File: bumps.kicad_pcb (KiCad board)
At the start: 2 copper layers, 111.1 x 65.4 mm, 132 parts, among them M1 CONN_1, M2 CONN_1, M3 CONN_1, P1 DIL6, P10 Mot-A, P11 Mot-A, P12 Mot-X, P13 T1, P14 T2, P15 T3, P16 MPower, P17 PWM-2, P18 PWM-1, P19 END-X, P2 DIL6, P20 END-Y, P21 END-Z, P22 Mot-X, P23 Mot-Y, P24 Mot-Y, P25 Mot-Z, P26 Mot-Z, P27 Aux, P28 KillSwitch, P29 PWM, P3 Mot-E, P4 Mot-E, P5 DIL6, P6 DIL6, P7 DIL6, P8 P8 Header, P9 P9 Header, Q1 IRLB8743PBF, Q2 IRLB8743PBF, Q3 FDS9926A, Q4 FDS9926A, U1 Motor-2, U2 Motor-4, U3 Motor-5, U4 Motor-3, U5 Motor-1, U6 MC34063, U7 AP1117/3.3, U8 Opto

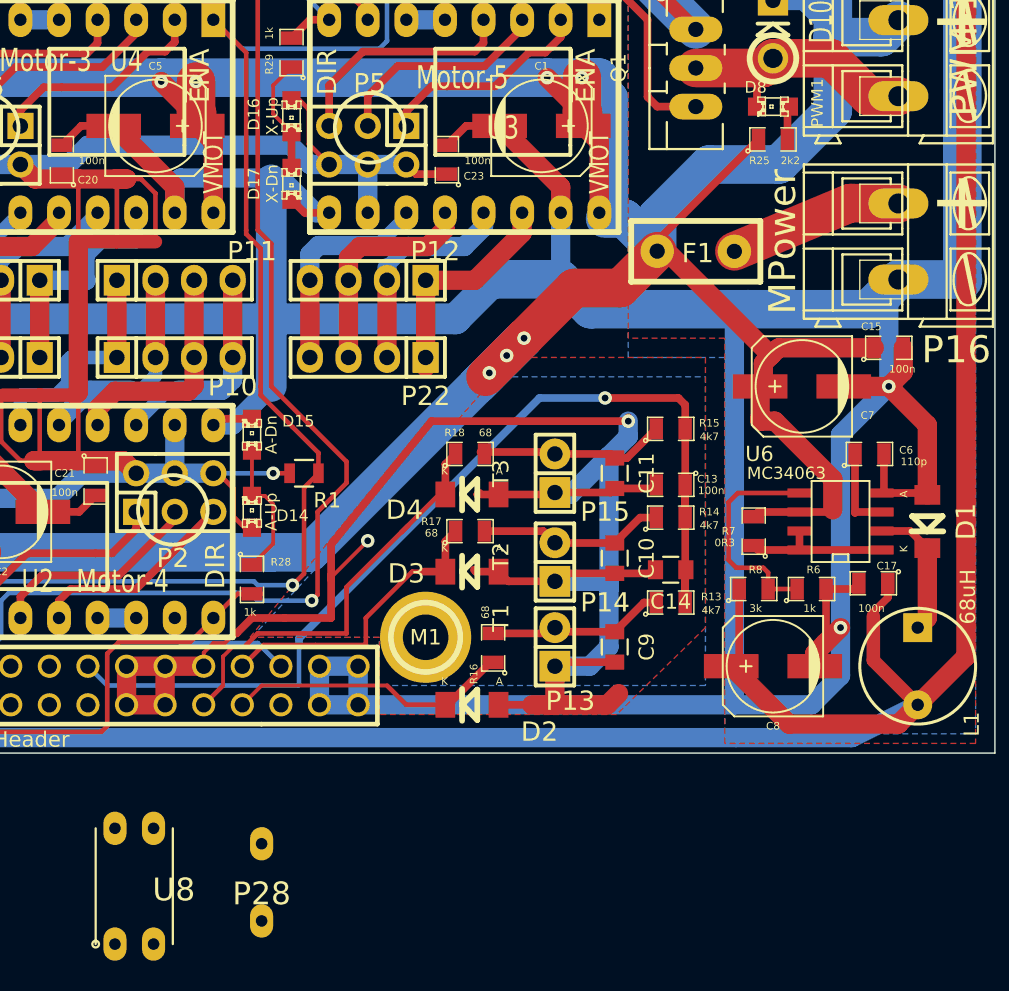
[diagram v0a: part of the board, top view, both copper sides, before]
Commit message: o Adding fuse holder (footprint and schematic). o .. work in progress. Attempt to make things fit.
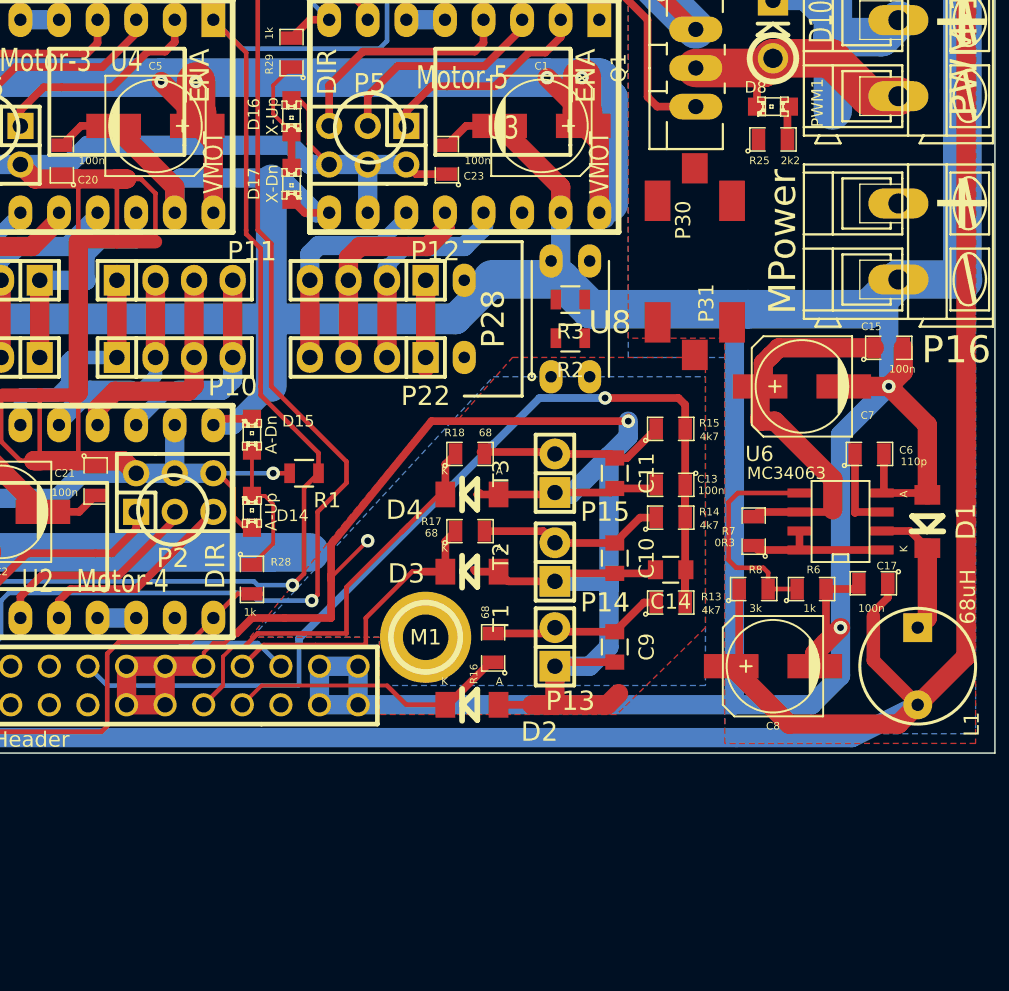
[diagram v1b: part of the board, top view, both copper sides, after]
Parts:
- removed F1: FUSE, Fuse_Holders_and_Fuses:Fuse_TE5_Littlefuse-395Series
- added P30: CONN_01X01, bumps:FuseBlade, F.Cu at (139.0, 57.0)
- added P31: CONN_01X01, bumps:FuseBlade, F.Cu at (139.0, 65.0)
- added R2: 330, Resistors_SMD:R_0805, F.Cu at (130.8, 66.0)
- added R3: 4k7, Resistors_SMD:R_0805, F.Cu at (130.8, 63.5)
- moved U8 47.1 mm to (130.8, 64.8)
- moved P28 39.4 mm to (123.8, 64.8), turned to 180 degrees
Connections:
- M1 pad 1: (no net) -> Net-(M1-Pad1)
- M2 pad 1: (no net) -> Net-(M2-Pad1)
- M3 pad 1: (no net) -> Net-(M3-Pad1)
- P8 pad 18: (no net) -> Net-(P8-Pad18)
- P8 pad 19: (no net) -> Net-(P8-Pad19)
- P8 pad 20: (no net) -> Net-(P8-Pad20)
- P8 pad 21: (no net) -> Net-(P8-Pad21)
- P8 pad 22: (no net) -> Net-(P8-Pad22)
- P8 pad 23: (no net) -> Net-(P8-Pad23)
- P8 pad 24: (no net) -> Net-(P8-Pad24)
- P8 pad 25: (no net) -> Net-(P8-Pad25)
- P8 pad 26: (no net) -> Net-(P8-Pad26)
- P8 pad 27: (no net) -> Net-(P8-Pad27)
- P8 pad 28: (no net) -> Net-(P8-Pad28)
- P8 pad 29: (no net) -> Net-(P8-Pad29)
- P8 pad 3: (no net) -> Net-(P8-Pad3)
- P8 pad 30: (no net) -> Net-(P8-Pad30)
- P8 pad 31: (no net) -> Net-(P8-Pad31)
- P8 pad 32: (no net) -> Net-(P8-Pad32)
- P8 pad 33: (no net) -> Net-(P8-Pad33)
- P8 pad 34: (no net) -> Net-(P8-Pad34)
- P8 pad 35: (no net) -> Net-(P8-Pad35)
- P8 pad 36: (no net) -> Net-(P8-Pad36)
- P8 pad 37: (no net) -> Net-(P8-Pad37)
- P8 pad 38: (no net) -> Net-(P8-Pad38)
- P8 pad 39: (no net) -> Net-(P8-Pad39)
- P8 pad 4: (no net) -> Net-(P8-Pad4)
- P8 pad 40: (no net) -> Net-(P8-Pad40)
- P8 pad 41: (no net) -> Net-(P8-Pad41)
- P8 pad 42: (no net) -> Net-(P8-Pad42)
- P8 pad 43: (no net) -> Net-(P8-Pad43)
- P8 pad 44: (no net) -> Net-(P8-Pad44)
- P8 pad 45: (no net) -> Net-(P8-Pad45)
- P8 pad 46: (no net) -> Net-(P8-Pad46)
- P8 pad 5: (no net) -> Net-(P8-Pad5)
- P8 pad 6: (no net) -> Net-(P8-Pad6)
- P9 pad 10: (no net) -> Net-(P9-Pad10)
- P9 pad 14: (no net) -> DIR_C
- P9 pad 16: (no net) -> DIR_U
- P9 pad 19: (no net) -> Net-(P9-Pad19)
- P9 pad 20: (no net) -> Net-(P9-Pad20)
- P9 pad 23: (no net) -> DIR_B
- P9 pad 24: (no net) -> STEP_C
- P9 pad 25: (no net) -> Net-(P9-Pad25)
- P9 pad 26: (no net) -> STEP_B
- P9 pad 27: (no net) -> Net-(P9-Pad27)
- P9 pad 28: (no net) -> Net-(P9-Pad28)
- P9 pad 29: (no net) -> Net-(P9-Pad29)
- P9 pad 3: (no net) -> Net-(P9-Pad3)
- P9 pad 30: (no net) -> Net-(P9-Pad30)
- P9 pad 31: (no net) -> Net-(P9-Pad31)
- P9 pad 4: (no net) -> Net-(P9-Pad4)
- P9 pad 41: (no net) -> STEP_U
- P9 pad 7: (no net) -> Net-(P9-Pad7)
- P9 pad 8: (no net) -> Net-(P9-Pad8)
- P9 pad 9: (no net) -> Net-(P9-Pad9)
- U8 pad 1: (no net) -> Net-(R2-Pad2)
- U8 pad 3: (no net) -> ~EStop
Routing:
- net VMOT: track 329.1 -> 247.3 mm, vias 13 -> 10
- net Net-(P16-Pad1): track 11.4 -> 0.00 mm
- net Net-(P12-Pad1): track 14.7 -> 5.71 mm

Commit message: o intermediate state.
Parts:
- U8: moved to B.Cu
- turned P28 to 0 degrees
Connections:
- M1 pad 1: Net-(M1-Pad1) -> (no net)
- M2 pad 1: Net-(M2-Pad1) -> (no net)
- M3 pad 1: Net-(M3-Pad1) -> (no net)
- P8 pad 18: Net-(P8-Pad18) -> (no net)
- P8 pad 19: Net-(P8-Pad19) -> (no net)
- P8 pad 20: Net-(P8-Pad20) -> (no net)
- P8 pad 21: Net-(P8-Pad21) -> (no net)
- P8 pad 22: Net-(P8-Pad22) -> (no net)
- P8 pad 23: Net-(P8-Pad23) -> (no net)
- P8 pad 24: Net-(P8-Pad24) -> (no net)
- P8 pad 25: Net-(P8-Pad25) -> (no net)
- P8 pad 26: Net-(P8-Pad26) -> (no net)
- P8 pad 27: Net-(P8-Pad27) -> (no net)
- P8 pad 28: Net-(P8-Pad28) -> (no net)
- P8 pad 29: Net-(P8-Pad29) -> (no net)
- P8 pad 3: Net-(P8-Pad3) -> (no net)
- P8 pad 30: Net-(P8-Pad30) -> (no net)
- P8 pad 31: Net-(P8-Pad31) -> (no net)
- P8 pad 32: Net-(P8-Pad32) -> (no net)
- P8 pad 33: Net-(P8-Pad33) -> (no net)
- P8 pad 34: Net-(P8-Pad34) -> (no net)
- P8 pad 35: Net-(P8-Pad35) -> (no net)
- P8 pad 36: Net-(P8-Pad36) -> (no net)
- P8 pad 37: Net-(P8-Pad37) -> (no net)
- P8 pad 38: Net-(P8-Pad38) -> (no net)
- P8 pad 39: Net-(P8-Pad39) -> (no net)
- P8 pad 4: Net-(P8-Pad4) -> (no net)
- P8 pad 40: Net-(P8-Pad40) -> (no net)
- P8 pad 41: Net-(P8-Pad41) -> (no net)
- P8 pad 42: Net-(P8-Pad42) -> (no net)
- P8 pad 43: Net-(P8-Pad43) -> (no net)
- P8 pad 44: Net-(P8-Pad44) -> (no net)
- P8 pad 45: Net-(P8-Pad45) -> (no net)
- P8 pad 46: Net-(P8-Pad46) -> (no net)
- P8 pad 5: Net-(P8-Pad5) -> (no net)
- P8 pad 6: Net-(P8-Pad6) -> (no net)
- P9 pad 10: Net-(P9-Pad10) -> (no net)
- P9 pad 14: DIR_C -> (no net)
- P9 pad 16: DIR_U -> (no net)
- P9 pad 19: Net-(P9-Pad19) -> (no net)
- P9 pad 20: Net-(P9-Pad20) -> (no net)
- P9 pad 23: DIR_B -> (no net)
- P9 pad 24: STEP_C -> (no net)
- P9 pad 25: Net-(P9-Pad25) -> (no net)
- P9 pad 26: STEP_B -> (no net)
- P9 pad 27: Net-(P9-Pad27) -> (no net)
- P9 pad 28: Net-(P9-Pad28) -> (no net)
- P9 pad 29: Net-(P9-Pad29) -> (no net)
- P9 pad 3: Net-(P9-Pad3) -> (no net)
- P9 pad 30: Net-(P9-Pad30) -> (no net)
- P9 pad 31: Net-(P9-Pad31) -> (no net)
- P9 pad 4: Net-(P9-Pad4) -> (no net)
- P9 pad 41: STEP_U -> (no net)
- P9 pad 7: Net-(P9-Pad7) -> (no net)
- P9 pad 8: Net-(P9-Pad8) -> (no net)
- P9 pad 9: Net-(P9-Pad9) -> (no net)
- U1 pad 5: Net-(U1-Pad5) -> ~EStop
- U1 pad 6: Net-(U1-Pad5) -> (no net)
- U2 pad 5: Net-(U2-Pad5) -> ~EStop
- U2 pad 6: Net-(U2-Pad5) -> (no net)
- U3 pad 5: Net-(U3-Pad5) -> ~EStop
- U3 pad 6: Net-(U3-Pad5) -> (no net)
- U4 pad 5: Net-(U4-Pad5) -> ~EStop
- U4 pad 6: Net-(U4-Pad5) -> (no net)
- U5 pad 5: Net-(U5-Pad5) -> ~EStop
- U5 pad 6: Net-(U5-Pad5) -> (no net)
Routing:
- net Net-(U4-Pad5): track 2.54 -> 0.00 mm
- net Net-(U3-Pad5): track 2.54 -> 0.00 mm
- net Net-(U2-Pad5): track 2.54 -> 0.00 mm
- net Net-(U5-Pad5): track 2.54 -> 0.00 mm
- net Net-(U1-Pad5): track 2.54 -> 0.00 mm

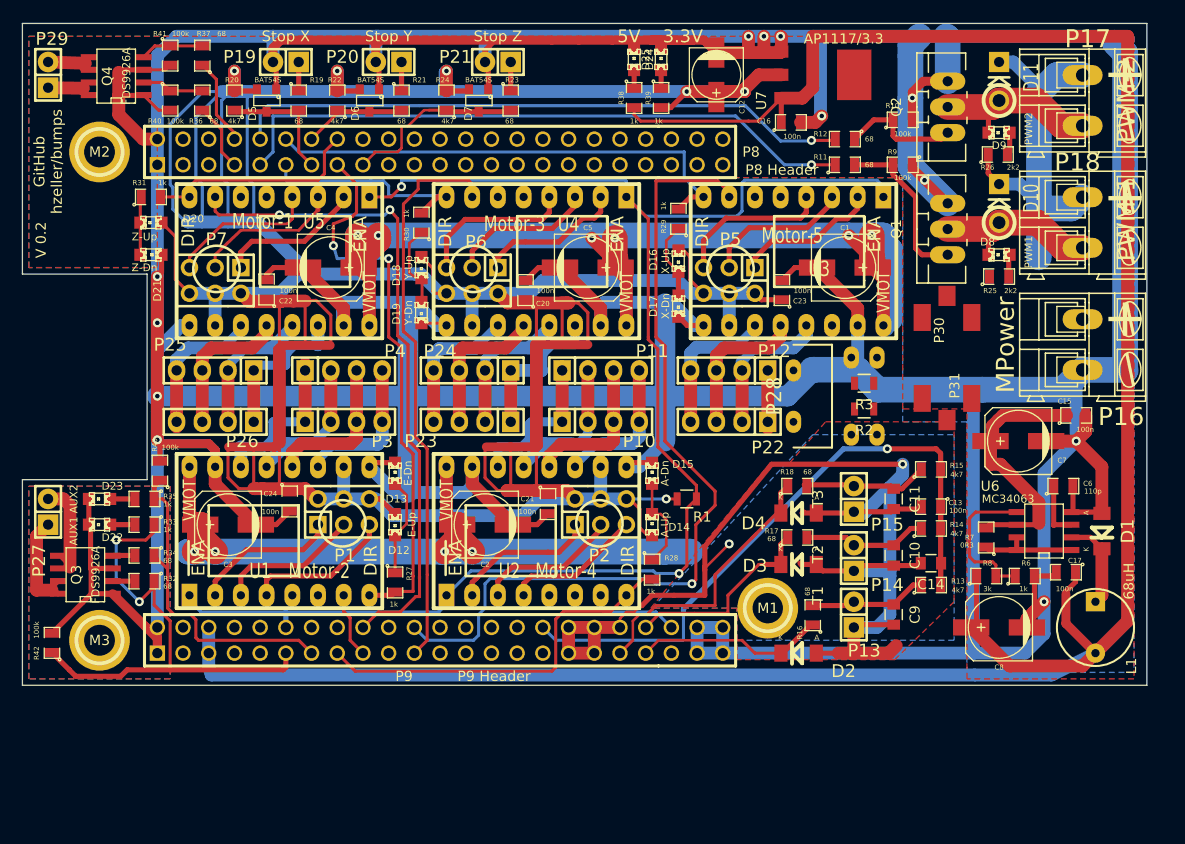
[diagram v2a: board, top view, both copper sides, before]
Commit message: o Bring to latest state of kicad library. o Now checking in also bumps-cache: learned that it   is effectively the 'project library' keeping track of   the symbols being used. o (was done in a branch, squashed together now).
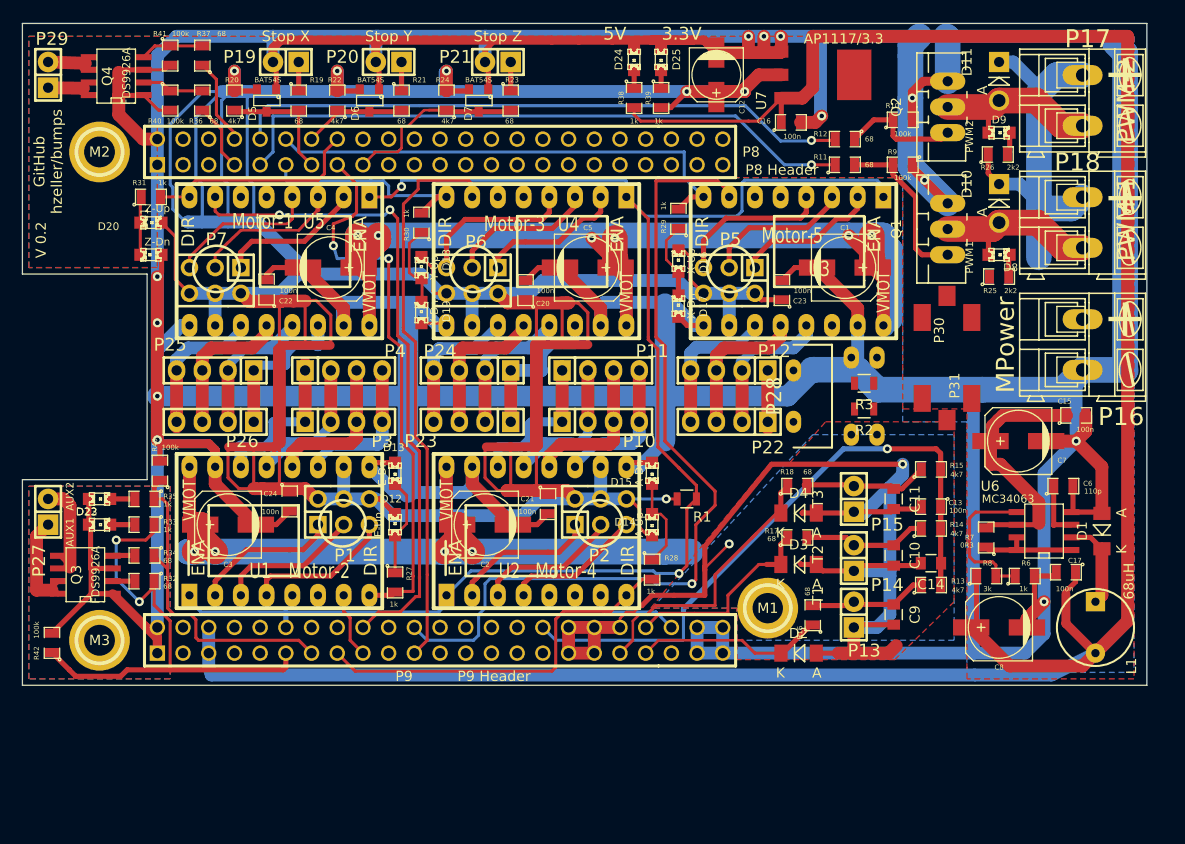
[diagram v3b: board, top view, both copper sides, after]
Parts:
- D10, D11: footprint Diodes_ThroughHole:Diode_DO-41_SOD81_Vertical_KathodeUp -> Diodes_ThroughHole:Diode_DO-41_SOD81_Vertical_AnodeUp
- Q1, Q2: footprint Transistors_TO-220:TO-220_FET-GDS_Vertical_LargePads -> Transistors_TO-220:TO-220_Neutral123_Vertical_LargePads
- moved D10 3.81 mm to (144.1, 43.8), turned to 270 degrees
- moved D11 3.81 mm to (144.1, 31.8), turned to 270 degrees
- turned D1 to 90 degrees
- turned D12 to 90 degrees
- turned D13 to 270 degrees
- turned D14 to 270 degrees
- turned D15 to 270 degrees
- turned D16 to 90 degrees
- turned D17 to 90 degrees
- turned D18 to 90 degrees
- turned D19 to 90 degrees
- turned D2 to 0 degrees
- turned D20 to 0 degrees
- turned D21 to 180 degrees
- turned D22 to 0 degrees
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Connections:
- D1 pad 1: GND -> Net-(D1-Pad1)
- D1 pad 2: Net-(D1-Pad2) -> GND
- D10 pad 1: Net-(D10-Pad1) -> VMOT
- D10 pad 2: VMOT -> Net-(D10-Pad2)
- D11 pad 1: Net-(D11-Pad1) -> VMOT
- D11 pad 2: VMOT -> Net-(D11-Pad2)
- D12 pad 1: VDD_3V3 -> Net-(D12-Pad1)
- D12 pad 2: Net-(D12-Pad2) -> VDD_3V3
- D13 pad 1: Net-(D12-Pad2) -> GND
- D13 pad 2: GND -> Net-(D12-Pad1)
- D14 pad 1: VDD_3V3 -> Net-(D14-Pad1)
- D14 pad 2: Net-(D14-Pad2) -> VDD_3V3
- D15 pad 1: Net-(D14-Pad2) -> GND
- D15 pad 2: GND -> Net-(D14-Pad1)
- D16 pad 1: VDD_3V3 -> Net-(D16-Pad1)
- D16 pad 2: Net-(D16-Pad2) -> VDD_3V3
- D17 pad 1: Net-(D16-Pad2) -> GND
- D17 pad 2: GND -> Net-(D16-Pad1)
- D18 pad 1: VDD_3V3 -> Net-(D18-Pad1)
- D18 pad 2: Net-(D18-Pad2) -> VDD_3V3
- D19 pad 1: Net-(D18-Pad2) -> GND
- D19 pad 2: GND -> Net-(D18-Pad1)
- D2 pad 1: AGND -> TEMP_1
- D2 pad 2: TEMP_1 -> AGND
- D20 pad 1: VDD_3V3 -> Net-(D20-Pad1)
- D20 pad 2: Net-(D20-Pad2) -> VDD_3V3
- D21 pad 1: Net-(D20-Pad2) -> GND
- D21 pad 2: GND -> Net-(D20-Pad1)
- D22 pad 1: Net-(D22-Pad1) -> GND
- D22 pad 2: GND -> Net-(D22-Pad2)
- D23 pad 1: Net-(D23-Pad1) -> GND
- D23 pad 2: GND -> Net-(D23-Pad2)
- D24 pad 1: Net-(D24-Pad1) -> GND
- D24 pad 2: GND -> Net-(D24-Pad2)
- D25 pad 1: Net-(D25-Pad1) -> GND
- D25 pad 2: GND -> Net-(D25-Pad2)
- D3 pad 1: AGND -> TEMP_2
- D3 pad 2: TEMP_2 -> AGND
- D4 pad 1: AGND -> TEMP_3
- D4 pad 2: TEMP_3 -> AGND
- D8 pad 1: Net-(D8-Pad1) -> Net-(D10-Pad2)
- D8 pad 2: Net-(D10-Pad1) -> Net-(D8-Pad2)
- D9 pad 1: Net-(D9-Pad1) -> Net-(D11-Pad2)
- D9 pad 2: Net-(D11-Pad1) -> Net-(D9-Pad2)
- L1 pad 1: Net-(D1-Pad2) -> Net-(D1-Pad1)
- P17 pad 2: Net-(D11-Pad1) -> Net-(D11-Pad2)
- P18 pad 2: Net-(D10-Pad1) -> Net-(D10-Pad2)
- R10 pad 1: Net-(Q2-PadG) -> Net-(Q2-Pad1)
- R11 pad 2: Net-(Q1-PadG) -> Net-(Q1-Pad1)
- R12 pad 1: Net-(Q2-PadG) -> Net-(Q2-Pad1)
- R25 pad 2: Net-(D8-Pad1) -> Net-(D8-Pad2)
- R26 pad 2: Net-(D9-Pad1) -> Net-(D9-Pad2)
- R27 pad 1: Net-(D12-Pad2) -> Net-(D12-Pad1)
- R28 pad 1: Net-(D14-Pad2) -> Net-(D14-Pad1)
- R29 pad 1: Net-(D16-Pad2) -> Net-(D16-Pad1)
- R30 pad 1: Net-(D18-Pad2) -> Net-(D18-Pad1)
- R31 pad 1: Net-(D20-Pad2) -> Net-(D20-Pad1)
- R33 pad 2: Net-(D22-Pad1) -> Net-(D22-Pad2)
- R35 pad 2: Net-(D23-Pad1) -> Net-(D23-Pad2)
- R38 pad 1: Net-(D24-Pad1) -> Net-(D24-Pad2)
- R39 pad 1: Net-(D25-Pad1) -> Net-(D25-Pad2)
- R9 pad 2: Net-(Q1-PadG) -> Net-(Q1-Pad1)
- U6 pad 2: Net-(D1-Pad2) -> Net-(D1-Pad1)
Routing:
- net Net-(D10-Pad2): track 0.00 -> 18.2 mm
- net Net-(D10-Pad1): track 18.2 -> 0.00 mm
- net Net-(D11-Pad2): track 0.00 -> 18.2 mm
- net Net-(D11-Pad1): track 18.2 -> 0.00 mm
- net Net-(Q1-PadG): track 16.4 -> 0.00 mm
- net Net-(Q1-Pad1): track 0.00 -> 16.4 mm
- net Net-(Q2-Pad1): track 0.00 -> 12.0 mm
- net Net-(Q2-PadG): track 12.0 -> 0.00 mm
- net Net-(D12-Pad1): track 0.00 -> 9.74 mm
- net Net-(D12-Pad2): track 9.74 -> 0.00 mm
- net Net-(D14-Pad1): track 0.00 -> 9.18 mm
- net Net-(D14-Pad2): track 9.18 -> 0.00 mm
- net Net-(D1-Pad2): track 8.98 -> 0.00 mm
- net Net-(D1-Pad1): track 0.00 -> 8.98 mm
- net Net-(D18-Pad2): track 8.38 -> 0.00 mm
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
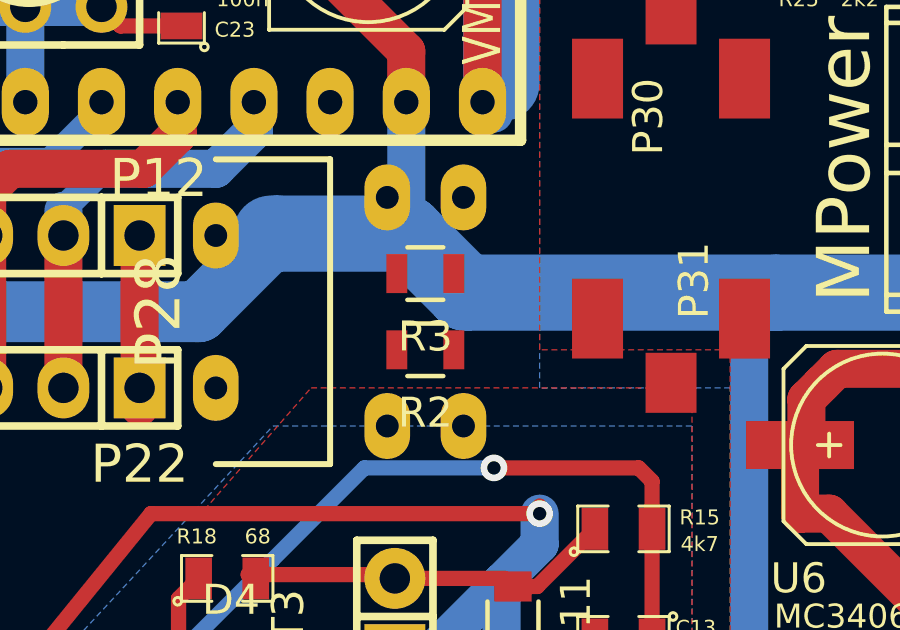
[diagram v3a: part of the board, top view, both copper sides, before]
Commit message: o use standard opto PC817 footprint.
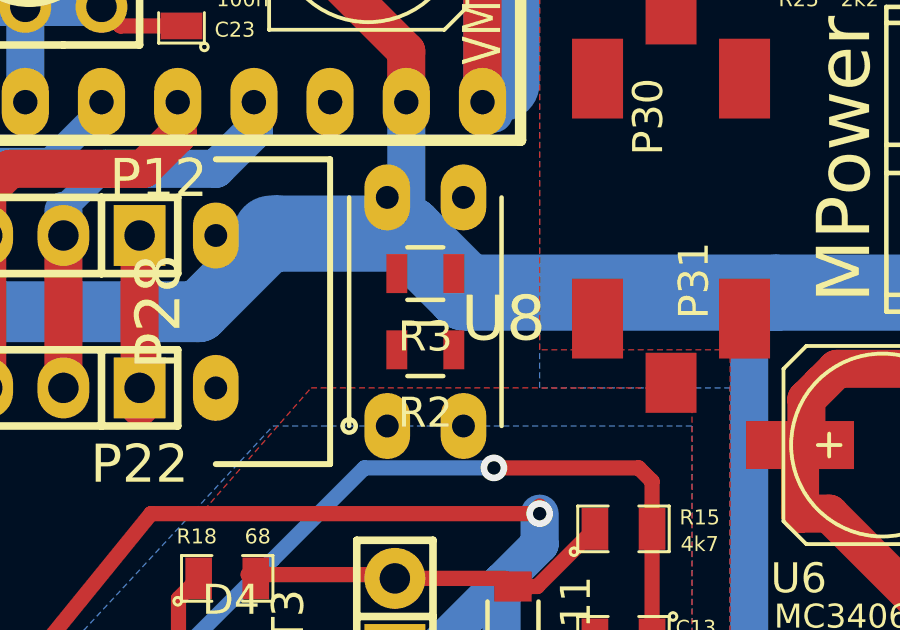
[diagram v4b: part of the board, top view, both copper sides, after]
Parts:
- U8: value Opto -> PC817; moved to F.Cu
